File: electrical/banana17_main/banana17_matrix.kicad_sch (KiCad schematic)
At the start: 1 part, among them SW1 SW

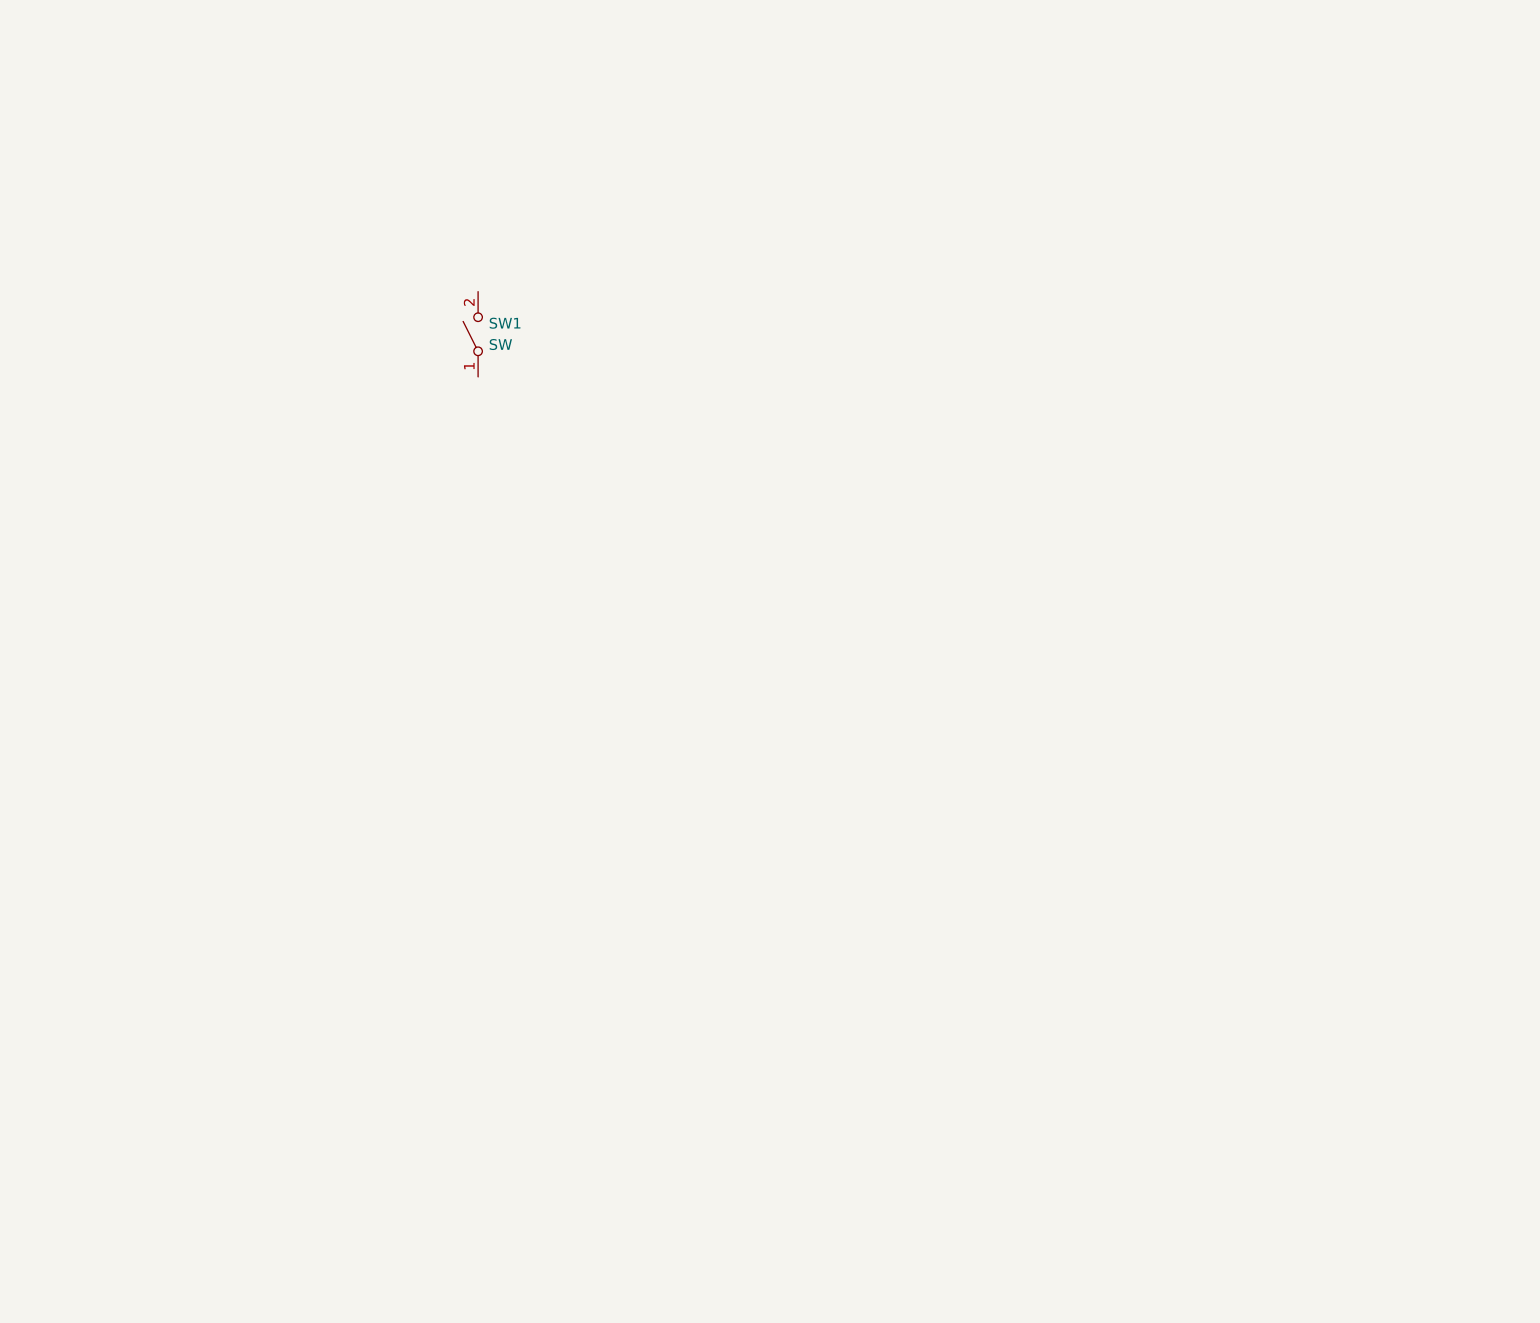
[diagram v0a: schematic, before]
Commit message: Matrix schematic complete
Matrix schematic complete.
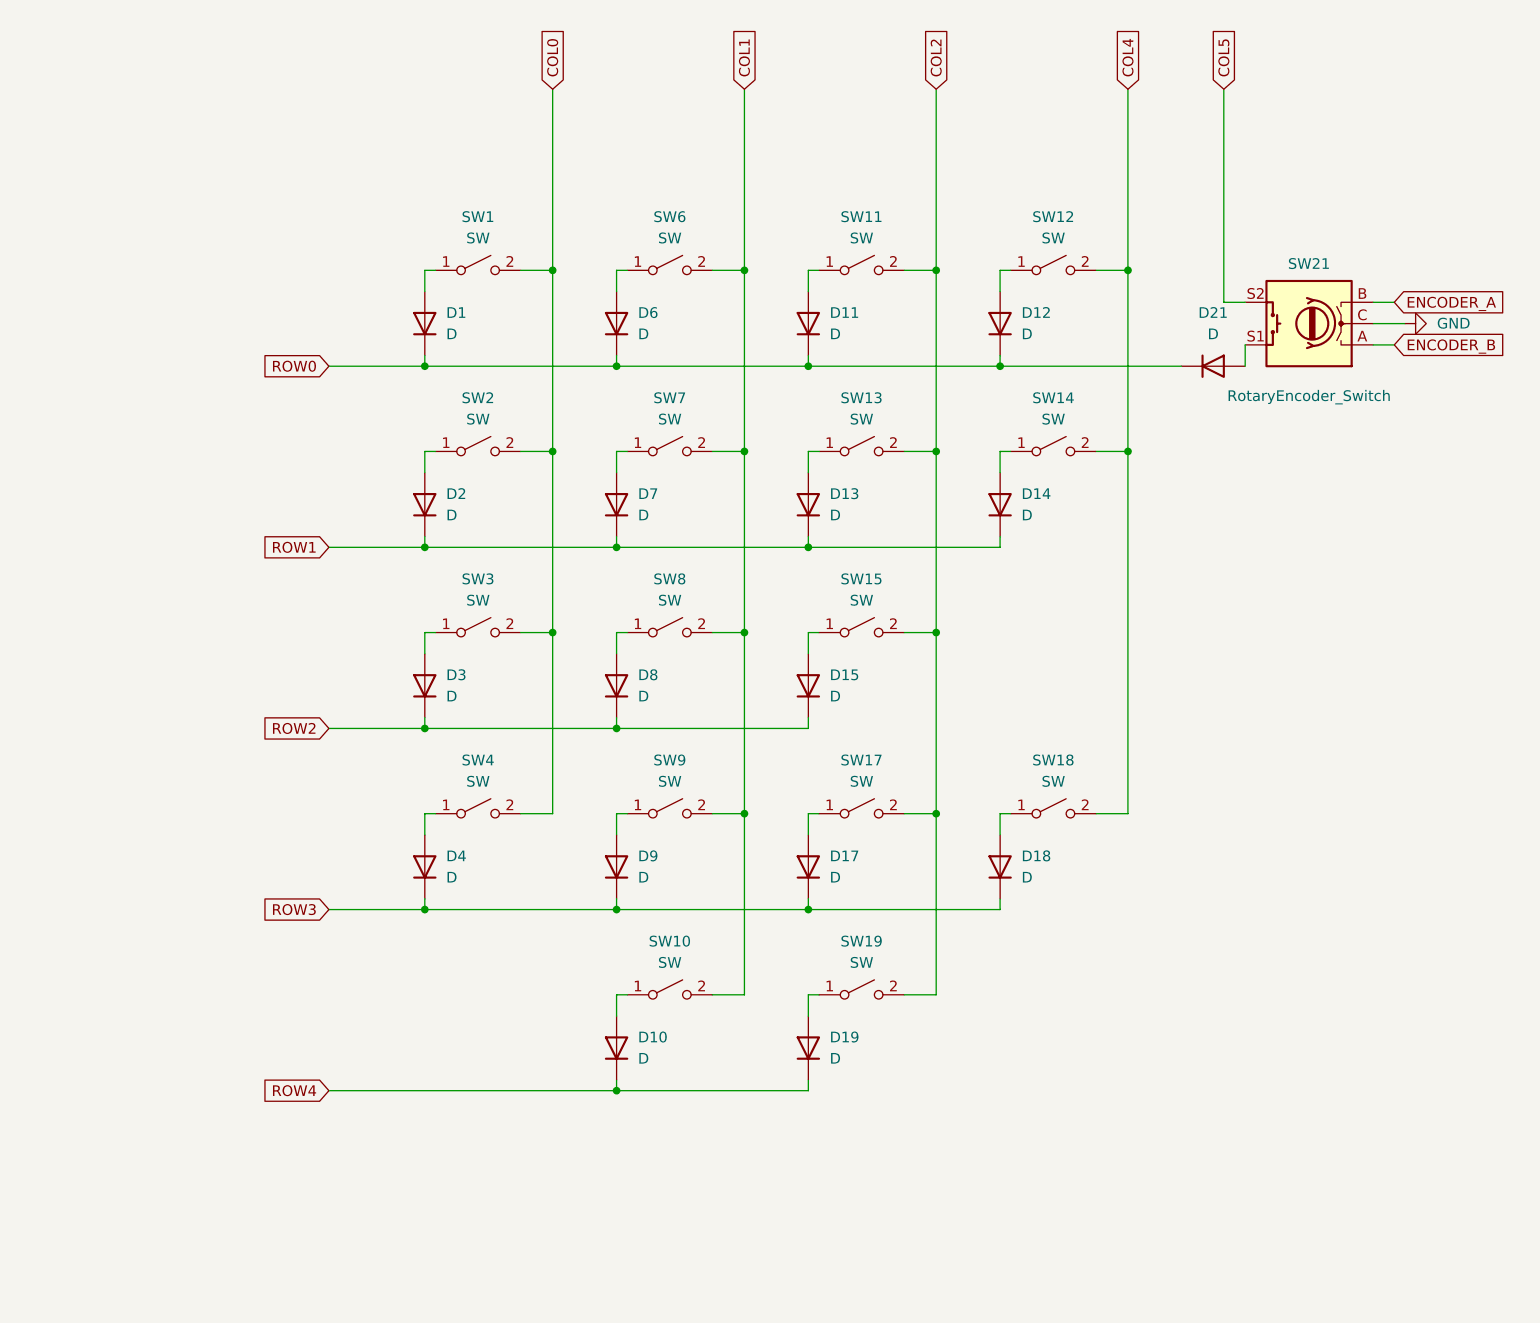
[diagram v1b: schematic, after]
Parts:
- added D1, D10, D11, D12, D13, D14, D15, D17, D18, D19, D2, D21, D3, D4, D6, D7, D8, D9: D, symbol Device:D
- added SW10, SW11, SW12, SW13, SW14, SW15, SW17, SW18, SW19, SW2, SW3, SW4, SW6, SW7, SW8, SW9: SW, symbol Switch:SW_SPST
- added SW21: RotaryEncoder_Switch, symbol Device:RotaryEncoder_Switch
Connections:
- net at SW1.1 (A): now also D1.2 (A)
- net COL0: now reaches SW1.2 (B)
- net COL0: now also SW2.2 (B), SW3.2 (B), SW4.2 (B)
- new net: D17.2 (A), SW17.1 (A)
- new net: D4.2 (A), SW4.1 (A)
- new net: D11.2 (A), SW11.1 (A)
- new net: D8.2 (A), SW8.1 (A)
- new net: D14.2 (A), SW14.1 (A)
- new net: D18.2 (A), SW18.1 (A)
- new net: D10.2 (A), SW10.1 (A)
- new net: D3.2 (A), SW3.1 (A)
- new net: D21.2 (A), SW21.S1
- new net: D15.2 (A), SW15.1 (A)
- new net: D19.2 (A), SW19.1 (A)
- new net: D6.2 (A), SW6.1 (A)
- new net: D2.2 (A), SW2.1 (A)
- new net: D12.2 (A), SW12.1 (A)
- new net: D9.2 (A), SW9.1 (A)
- new net: D13.2 (A), SW13.1 (A)
- new net: D7.2 (A), SW7.1 (A)
- new net COL1: SW10.2 (B), SW6.2 (B), SW7.2 (B), SW8.2 (B), SW9.2 (B)
- new net COL2: SW11.2 (B), SW13.2 (B), SW15.2 (B), SW17.2 (B), SW19.2 (B)
- new net COL4: SW12.2 (B), SW14.2 (B), SW18.2 (B)
- new net COL5: SW21.S2
- new net ENCODER_A: SW21.B
- new net ENCODER_B: SW21.A
- new net GND: SW21.C
- new net ROW0: D1.1 (K), D11.1 (K), D12.1 (K), D21.1 (K), D6.1 (K)
- new net ROW1: D13.1 (K), D14.1 (K), D2.1 (K), D7.1 (K)
- new net ROW2: D15.1 (K), D3.1 (K), D8.1 (K)
- new net ROW3: D17.1 (K), D18.1 (K), D4.1 (K), D9.1 (K)
- new net ROW4: D10.1 (K), D19.1 (K)
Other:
- moved on the sheet: SW1

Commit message: Altered encoder placement on schematic.
Altered encoder placement on schematic.
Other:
- note added: "26/07/2024"
- note added: "Banana 17 Matrix"
- moved on the sheet: D21, SW21
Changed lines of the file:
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@@
 	)
 	(junction
+		(at 160.02 82.55)
+		(diameter 0)
+		(color 0 0 0 0)
+	)
+	(junction
 		(at 129.54 114.3)
 		(diameter 0)
@@
 	)
 	(junction
-		(at 160.02 82.55)
-		(diameter 0)
-		(color 0 0 0 0)
-	)
-	(junction
 		(at 152.4 114.3)
 		(diameter 0)
@@
 	(wire
 		(pts
-			(xy 189.23 74.93) (xy 186.69 74.93)
-		)
-		(stroke
-			(width 0)
-			(type default)
-		)
-	)
-	(wire
-		(pts
 			(xy 102.87 92.71) (xy 106.68 92.71)
 		)
@@
 	(wire
 		(pts
-			(xy 160.02 81.28) (xy 160.02 82.55)
-		)
-		(stroke
-			(width 0)
-			(type default)
-		)
-	)
-	(wire
-		(pts
 			(xy 171.45 71.12) (xy 175.26 71.12)
 		)
@@
 	(wire
 		(pts
-			(xy 189.23 80.01) (xy 189.23 82.55)
-		)
-		(stroke
-			(width 0)
-			(type default)
-		)
-	)
-	(wire
-		(pts
 			(xy 91.44 82.55) (xy 114.3 82.55)
 		)
@@
 	(wire
 		(pts
+			(xy 182.88 73.66) (xy 182.88 71.12)
+		)
+		(stroke
+			(width 0)
+			(type default)
+		)
+	)
+	(wire
+		(pts
 			(xy 102.87 135.89) (xy 106.68 135.89)
 		)
@@
 	(wire
 		(pts
+			(xy 160.02 82.55) (xy 160.02 81.28)
+		)
+		(stroke
+			(width 0)
+			(type default)
+		)
+	)
+	(wire
+		(pts
 			(xy 137.16 81.28) (xy 137.16 82.55)
 		)
@@
 	(wire
 		(pts
-			(xy 204.47 80.01) (xy 207.01 80.01)
+			(xy 193.04 86.36) (xy 193.04 88.9)
 		)
 		(stroke
@@
 	(wire
 		(pts
-			(xy 204.47 77.47) (xy 208.28 77.47)
+			(xy 195.58 86.36) (xy 195.58 90.17)
 		)
 		(stroke
@@
 	(wire
 		(pts
-			(xy 160.02 82.55) (xy 181.61 82.55)
+			(xy 160.02 82.55) (xy 182.88 82.55)
 		)
 		(stroke
@@
 	(wire
 		(pts
-			(xy 204.47 74.93) (xy 207.01 74.93)
+			(xy 198.12 86.36) (xy 198.12 88.9)
 		)
 		(stroke
@@
 	(wire
 		(pts
-			(xy 186.69 49.53) (xy 186.69 74.93)
+			(xy 198.12 49.53) (xy 198.12 71.12)
+		)
+		(stroke
+			(width 0)
+			(type default)
+		)
+	)
+	(wire
+		(pts
+			(xy 182.88 71.12) (xy 193.04 71.12)
+		)
+		(stroke
+			(width 0)
+			(type default)
+		)
+	)
+	(wire
+		(pts
+			(xy 182.88 82.55) (xy 182.88 81.28)
 		)
 		(stroke
@@
 		)
 	)
+	(text "26/07/2024"
+		(exclude_from_sim no)
+		(at 212.598 193.548 0)
+		(effects
+			(font
+				(size 1.27 1.27)
+			)
+		)
+	)
+	(text "Banana 17 Matrix"
+		(exclude_from_sim no)
+		(at 194.818 189.738 0)
+		(effects
+			(font
+				(size 1.27 1.27)
+			)
+		)
+	)
 	(global_label "COL4"
 		(shape input)
@@
 	(global_label "COL5"
 		(shape input)
-		(at 186.69 49.53 90)
+		(at 198.12 49.53 90)
 		(fields_autoplaced yes)
 		(effects
@@
 		)
 		(property "Intersheetrefs" "${INTERSHEET_REFS}"
-			(at 186.69 41.7067 90)
+			(at 198.12 41.7067 90)
 			(effects
 				(font
@@
 	(global_label "ENCODER_B"
 		(shape input)
-		(at 207.01 80.01 0)
+		(at 193.04 88.9 270)
 		(fields_autoplaced yes)
 		(effects
@@
 				(size 1.27 1.27)
 			)
-			(justify left)
+			(justify right)
 		)
 		(property "Intersheetrefs" "${INTERSHEET_REFS}"
-			(at 221.0018 80.01 0)
+			(at 193.04 102.8918 90)
 			(effects
 				(font
 					(size 1.27 1.27)
 				)
-				(justify left)
+				(justify right)
 				(hide yes)
 			)
@@
 	(global_label "ENCODER_A"
 		(shape input)
-		(at 207.01 74.93 0)
+		(at 198.12 88.9 270)
 		(fields_autoplaced yes)
 		(effects
@@
 				(size 1.27 1.27)
 			)
-			(justify left)
+			(justify right)
 		)
 		(property "Intersheetrefs" "${INTERSHEET_REFS}"
-			(at 220.8204 74.93 0)
+			(at 198.12 102.7104 90)
 			(effects
 				(font
 					(size 1.27 1.27)
 				)
-				(justify left)
+				(justify right)
 				(hide yes)
 			)
@@
 	(symbol
 		(lib_id "Device:D")
-		(at 185.42 82.55 0)
+		(at 182.88 77.47 90)
 		(unit 1)
 		(exclude_from_sim no)
@@
 		(fields_autoplaced yes)
 		(property "Reference" "D21"
-			(at 185.42 76.2 0)
+			(at 185.42 76.1999 90)
 			(effects
 				(font
 					(size 1.27 1.27)
 				)
+				(justify right)
 			)
 		)
 		(property "Value" "D"
-			(at 185.42 78.74 0)
+			(at 185.42 78.7399 90)
 			(effects
 				(font
 					(size 1.27 1.27)
 				)
+				(justify right)
 			)
 		)
 		(property "Footprint" ""
-			(at 185.42 82.55 0)
+			(at 182.88 77.47 0)
 			(effects
 				(font
@@
 		)
 		(property "Datasheet" "~"
-			(at 185.42 82.55 0)
+			(at 182.88 77.47 0)
 			(effects
 				(font
@@
 		)
 		(property "Description" "Diode"
-			(at 185.42 82.55 0)
+			(at 182.88 77.47 0)
 			(effects
 				(font
@@
 		)
 		(property "Sim.Device" "D"
-			(at 185.42 82.55 0)
+			(at 182.88 77.47 0)
 			(effects
 				(font
@@
 		)
 		(property "Sim.Pins" "1=K 2=A"
-			(at 185.42 82.55 0)
+			(at 182.88 77.47 0)
 			(effects
 				(font
@@
 	(symbol
 		(lib_id "power:GND")
-		(at 208.28 77.47 90)
+		(at 195.58 90.17 0)
 		(unit 1)
 		(exclude_from_sim no)
@@
 		(fields_autoplaced yes)
 		(property "Reference" "#PWR022"
-			(at 214.63 77.47 0)
+			(at 195.58 96.52 0)
 			(effects
 				(font
@@
 		)
 		(property "Value" "GND"
-			(at 212.09 77.4699 90)
+			(at 195.5801 93.98 90)
 			(effects
 				(font
@@
 		)
 		(property "Footprint" ""
-			(at 208.28 77.47 0)
+			(at 195.58 90.17 0)
 			(effects
 				(font
@@
 		)
 		(property "Datasheet" ""
-			(at 208.28 77.47 0)
+			(at 195.58 90.17 0)
 			(effects
 				(font
@@
 		)
 		(property "Description" "Power symbol creates a global label with name \"GND\" , ground"
-			(at 208.28 77.47 0)
+			(at 195.58 90.17 0)
 			(effects
 				(font
@@
 	(symbol
 		(lib_id "Device:RotaryEncoder_Switch")
-		(at 196.85 77.47 180)
+		(at 195.58 78.74 90)
 		(unit 1)
 		(exclude_from_sim no)
@@
 		(dnp no)
 		(property "Reference" "SW21"
-			(at 196.85 70.358 0)
+			(at 202.692 78.74 0)
 			(effects
 				(font
@@
 		)
 		(property "Value" "RotaryEncoder_Switch"
-			(at 196.85 86.106 0)
+			(at 195.58 105.918 90)
 			(effects
 				(font
@@
 		)
 		(property "Footprint" ""
-			(at 200.66 81.534 0)
+			(at 191.516 82.55 0)
 			(effects
 				(font
@@
 		)
 		(property "Datasheet" "~"
-			(at 196.85 84.074 0)
+			(at 188.976 78.74 0)
 			(effects
 				(font
@@
 		)
 		(property "Description" "Rotary encoder, dual channel, incremental quadrate outputs, with switch"
-			(at 196.85 77.47 0)
+			(at 195.58 78.74 0)
 			(effects
 				(font
